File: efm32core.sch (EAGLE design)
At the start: 44 parts, among them U1 IP4220CZ6SSOT-6, X1 48.0MHz, X2 32.768kHz

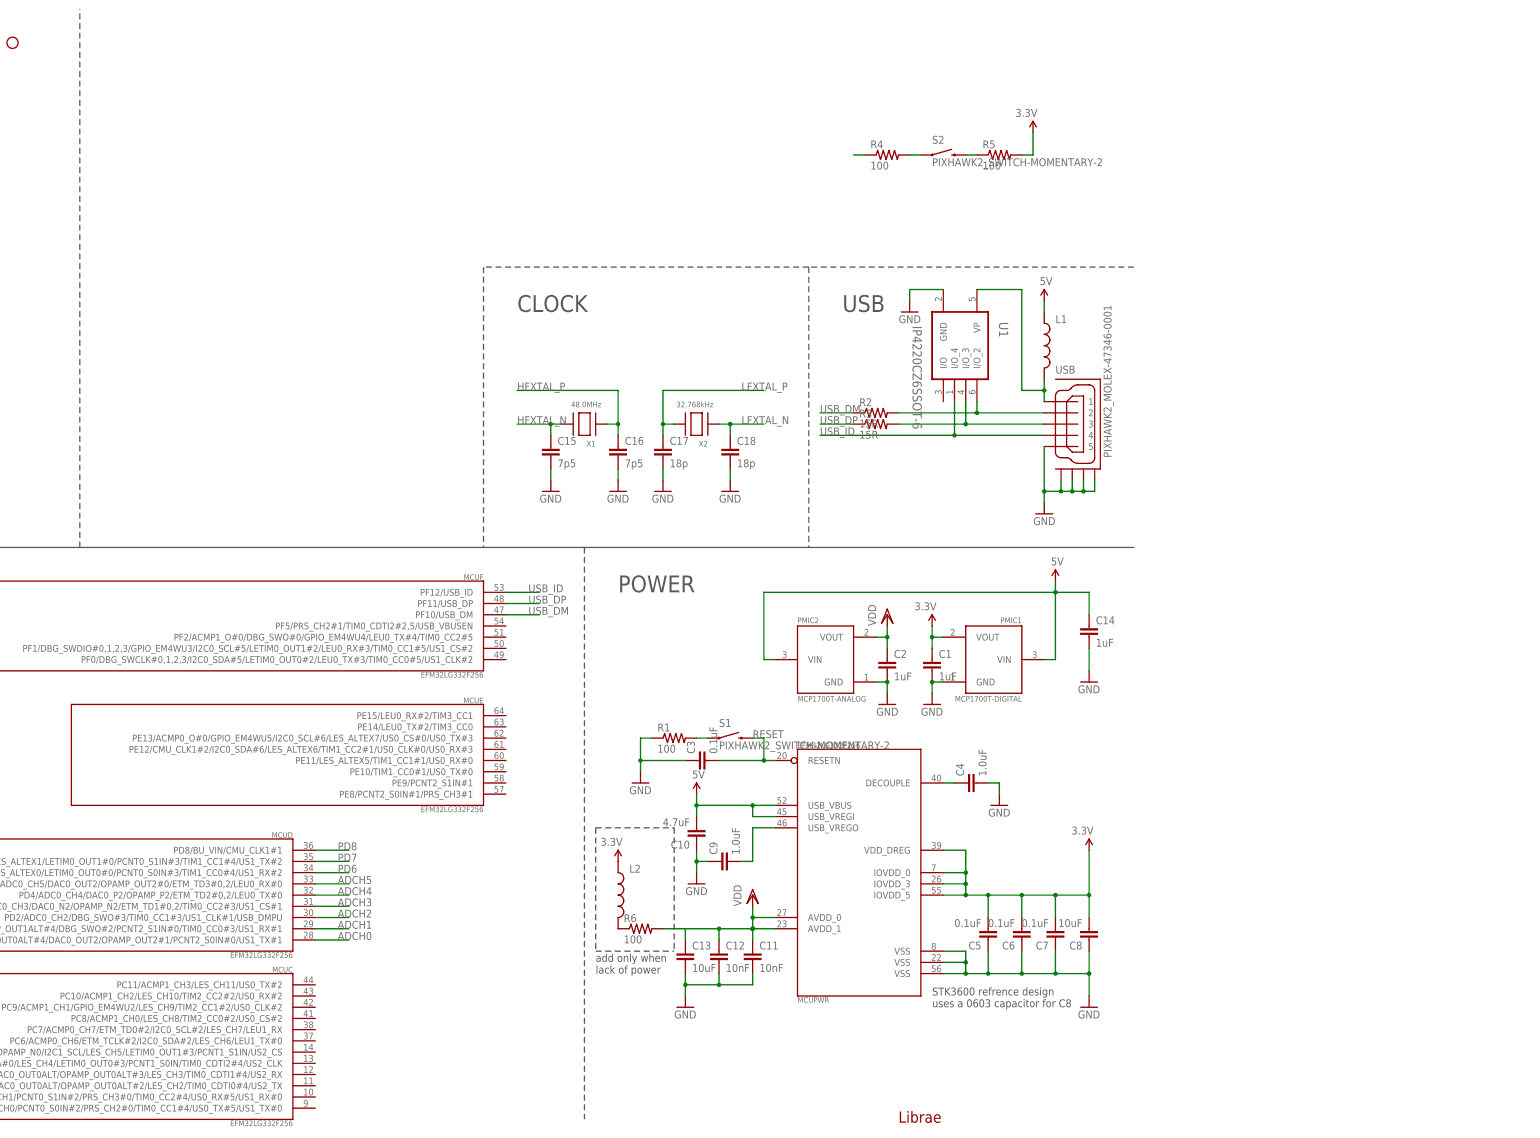
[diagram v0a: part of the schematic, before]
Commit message: add up bluetooth module and microsd socket
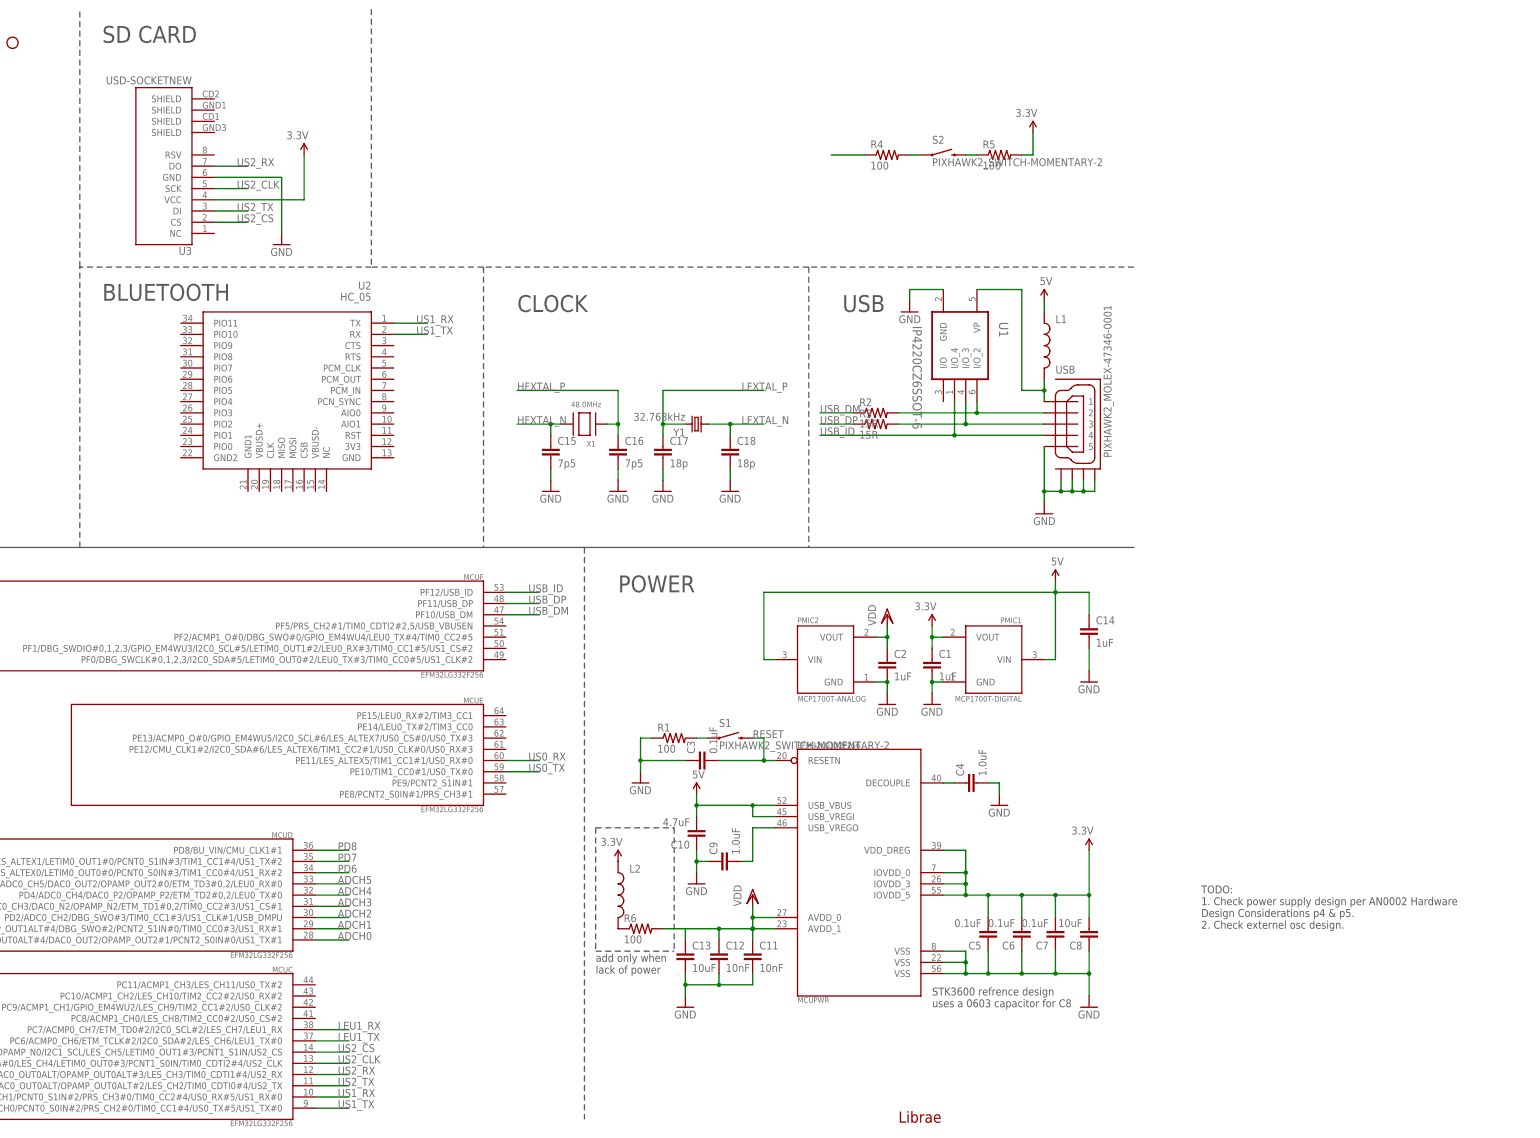
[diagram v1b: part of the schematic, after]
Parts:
- removed X2: 32.768kHz, adafruit:XTALNX5032
- added U2: HC_05, SerialPortBluetooth:HC_05
- added U3: USD-SOCKETNEW, SparkFun-Connectors:USD-SOCKETNEW
- added Y1: 32.768kHz, SparkFun-FreqCtrl:CRYSTAL5X1.5
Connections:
- new net LEU1_RX: MCUC.PC7/ACMP0_CH7/ETM_TD0#2/I2C0_SCL#2/LES_CH7/LEU1_RX
- new net LEU1_TX: MCUC.PC6/ACMP0_CH6/ETM_TCLK#2/I2C0_SDA#2/LES_CH6/LEU1_TX#0
- new net US0_RX: MCUE.PE11/LES_ALTEX5/TIM1_CC1#1/US0_RX#0
- new net US0_TX: MCUE.PE10/TIM1_CC0#1/US0_TX#0
- new net US1_RX: MCUC.PC1/ACMP0_CH1/DAC0_OUT0ALT/OPAMP_OUT0ALT#1/I2C0_SCL#4/LES_CH1/PCNT0_S1IN#2/PRS_CH3#0/TIM0_CC2#4/US0_RX#5/US1_RX#0, U2.TX
- new net US1_TX: MCUC.PC0/ACMP0_CH0/DAC0_OUT0ALT/OPAMP_OUT0ALT#0/I2C0_SDA#4/LES_CH0/PCNT0_S0IN#2/PRS_CH2#0/TIM0_CC1#4/US0_TX#5/US1_TX#0, U2.RX
- new net US2_CLK: MCUC.PC4/ACMP0_CH4/DAC0_P0/OPAMP_P0/I2C1_SDA#0/LES_CH4/LETIM0_OUT0#3/PCNT1_S0IN/TIM0_CDTI2#4/US2_CLK, U3.SCK
- new net US2_CS: MCUC.PC5/ACMP0_CH5/DAC0_N0/OPAMP_N0/I2C1_SCL/LES_CH5/LETIM0_OUT1#3/PCNT1_S1IN/US2_CS, U3.CS
- new net US2_RX: MCUC.PC3/ACMP0_CH3/DAC0_OUT0ALT/OPAMP_OUT0ALT#3/LES_CH3/TIM0_CDTI1#4/US2_RX, U3.DO
- new net US2_TX: MCUC.PC2/ACMP0_CH2/DAC0_OUT0ALT/OPAMP_OUT0ALT#2/LES_CH2/TIM0_CDTI0#4/US2_TX, U3.DI
- net 3.3V: now also U3.VCC
- net GND: now also U3.GND
- net LFXTAL_N: now also Y1.1; no longer X2.P$1
- net LFXTAL_P: now also Y1.2; no longer X2.P$2
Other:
- note added: "BLUETOOTH"
- note added: "SD CARD"
- note added: "TODO: 1. Check power supply design per AN0002 Hardware Design Considerations p4 & p5. 2. Check externel osc design."

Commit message: update a bit
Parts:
- added U4: MPU-6000QFN-24, SparkFun-Sensors:MPU-6000QFN-24
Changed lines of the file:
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@@
 <grid distance="0.1" unitdist="inch" unit="inch" style="lines" multiple="1" display="yes" altdistance="0.01" altunitdist="inch" altunit="inch"/>
 <layers>
-<layer number="1" name="Top" color="4" fill="1" visible="no" active="no"/>
-<layer number="16" name="Bottom" color="1" fill="1" visible="no" active="no"/>
-<layer number="17" name="Pads" color="2" fill="1" visible="no" active="no"/>
-<layer number="18" name="Vias" color="2" fill="1" visible="no" active="no"/>
-<layer number="19" name="Unrouted" color="6" fill="1" visible="no" active="no"/>
-<layer number="20" name="Dimension" color="15" fill="1" visible="no" active="no"/>
-<layer number="21" name="tPlace" color="7" fill="1" visible="no" active="no"/>
-<layer number="22" name="bPlace" color="7" fill="1" visible="no" active="no"/>
-<layer number="23" name="tOrigins" color="15" fill="1" visible="no" active="no"/>
-<layer number="24" name="bOrigins" color="15" fill="1" visible="no" active="no"/>
-<layer number="25" name="tNames" color="7" fill="1" visible="no" active="no"/>
-<layer number="26" name="bNames" color="7" fill="1" visible="no" active="no"/>
-<layer number="27" name="tValues" color="7" fill="1" visible="no" active="no"/>
-<layer number="28" name="bValues" color="7" fill="1" visible="no" active="no"/>
+<layer number="1" name="Top" color="4" fill="1" visible="yes" active="no"/>
+<layer number="16" name="Bottom" color="1" fill="1" visible="yes" active="no"/>
+<layer number="17" name="Pads" color="2" fill="1" visible="yes" active="no"/>
+<layer number="18" name="Vias" color="2" fill="1" visible="yes" active="no"/>
+<layer number="19" name="Unrouted" color="6" fill="1" visible="yes" active="no"/>
+<layer number="20" name="Dimension" color="15" fill="1" visible="yes" active="no"/>
+<layer number="21" name="tPlace" color="7" fill="1" visible="yes" active="no"/>
+<layer number="22" name="bPlace" color="7" fill="1" visible="yes" active="no"/>
+<layer number="23" name="tOrigins" color="15" fill="1" visible="yes" active="no"/>
+<layer number="24" name="bOrigins" color="15" fill="1" visible="yes" active="no"/>
+<layer number="25" name="tNames" color="7" fill="1" visible="yes" active="no"/>
+<layer number="26" name="bNames" color="7" fill="1" visible="yes" active="no"/>
+<layer number="27" name="tValues" color="7" fill="1" visible="yes" active="no"/>
+<layer number="28" name="bValues" color="7" fill="1" visible="yes" active="no"/>
 <layer number="29" name="tStop" color="7" fill="3" visible="no" active="no"/>
 <layer number="30" name="bStop" color="7" fill="6" visible="no" active="no"/>
@@
 <layer number="35" name="tGlue" color="7" fill="4" visible="no" active="no"/>
 <layer number="36" name="bGlue" color="7" fill="5" visible="no" active="no"/>
-<layer number="37" name="tTest" color="7" fill="1" visible="no" active="no"/>
-<layer number="38" name="bTest" color="7" fill="1" visible="no" active="no"/>
+<layer number="37" name="tTest" color="7" fill="1" visible="yes" active="no"/>
+<layer number="38" name="bTest" color="7" fill="1" visible="yes" active="no"/>
 <layer number="39" name="tKeepout" color="4" fill="11" visible="no" active="no"/>
 <layer number="40" name="bKeepout" color="1" fill="11" visible="no" active="no"/>
@@
 <layer number="44" name="Drills" color="7" fill="1" visible="no" active="no"/>
 <layer number="45" name="Holes" color="7" fill="1" visible="no" active="no"/>
-<layer number="46" name="Milling" color="3" fill="1" visible="no" active="no"/>
-<layer number="47" name="Measures" color="7" fill="1" visible="no" active="no"/>
-<layer number="48" name="Document" color="7" fill="1" visible="no" active="no"/>
-<layer number="49" name="Reference" color="7" fill="1" visible="no" active="no"/>
-<layer number="50" name="dxf" color="7" fill="1" visible="no" active="no"/>
-<layer number="51" name="tDocu" color="14" fill="1" visible="no" active="no"/>
-<layer number="52" name="bDocu" color="6" fill="1" visible="no" active="no"/>
-<layer number="53" name="tGND_GNDA" color="7" fill="9" visible="no" active="no"/>
-<layer number="54" name="bGND_GNDA" color="1" fill="9" visible="no" active="no"/>
-<layer number="56" name="wert" color="7" fill="1" visible="no" active="no"/>
-<layer number="57" name="tCAD" color="7" fill="1" visible="no" active="no"/>
-<layer number="58" name="bCAD" color="7" fill="1" visible="no" active="no"/>
+<layer number="46" name="Milling" color="3" fill="1" visible="yes" active="no"/>
+<layer number="47" name="Measures" color="7" fill="1" visible="yes" active="no"/>
+<layer number="48" name="Document" color="7" fill="1" visible="yes" active="no"/>
+<layer number="49" name="Reference" color="7" fill="1" visible="yes" active="no"/>
+<layer number="50" name="dxf" color="7" fill="1" visible="yes" active="no"/>
+<layer number="51" name="tDocu" color="14" fill="1" visible="yes" active="no"/>
+<layer number="52" name="bDocu" color="6" fill="1" visible="yes" active="no"/>
+<layer number="53" name="tGND_GNDA" color="7" fill="9" visible="yes" active="no"/>
+<layer number="54" name="bGND_GNDA" color="1" fill="9" visible="yes" active="no"/>
+<layer number="56" name="wert" color="7" fill="1" visible="yes" active="no"/>
+<layer number="57" name="tCAD" color="7" fill="1" visible="yes" active="no"/>
+<layer number="58" name="bCAD" color="7" fill="1" visible="yes" active="no"/>
 <layer number="91" name="Nets" color="2" fill="1" visible="yes" active="yes"/>
 <layer number="92" name="Busses" color="1" fill="1" visible="yes" active="yes"/>
@@
 <part name="GND15" library="SparkFun-Aesthetics" deviceset="GND" device=""/>
 <part name="3.3V4" library="SparkFun-Aesthetics" deviceset="3.3V" device=""/>
+<part name="U4" library="SparkFun-Sensors" deviceset="MPU-6000" device="QFN-24"/>
 </parts>
 <sheets>
@@
 <instance part="GND15" gate="1" x="190.5" y="203.2"/>
 <instance part="3.3V4" gate="G$1" x="195.58" y="223.52" rot="MR0"/>
+<instance part="U4" gate="G$1" x="243.84" y="231.14"/>
 </instances>
 <busses>

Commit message: complete connections
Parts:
- removed U4: MPU-6000QFN-24, SparkFun-Sensors:MPU-6000QFN-24
- added C19: 10nF, SparkFun-Capacitors:10NF/10000PF-50V-10%(0603)
- added C20, C21: 0.1uF, SparkFun-Capacitors:0.1UF-25V(+80/-20%)(0603)
- added C22: 2.2uF, SparkFun-Capacitors:2.2UF-10V-20%(0603)
- added MPU9150: (no value), SparkFun-Sensors:MPU-9150QFN-24-NP
- added R7, R8: 4.7k, SparkFun-Resistors:100OHM1/10W1%(0603)
- R4: value 100 -> 10k
- R5: value 100 -> 1k
- S2: value PIXHAWK2_SWITCH-MOMENTARY-2 -> BUTTON
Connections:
- removed net N$2: R4.2, S2.1
- removed net N$5: R4.1
- removed net PA0: MCUA.PA0/GPIO_EM4WU0/I2C0_SDA#0/LEU0_RX#4/PRS_CH0/TIM0_CC0#0,1,4
- new net I2C0_SCL: MCUA.PA1/CMU_CLK1#0/I2C0_SCL#0/PRS_CH1/TIM0_CC1#0,1, MPU9150.SCL, R8.1
- new net I2C0_SDA: MCUA.PA0/GPIO_EM4WU0/I2C0_SDA#0/LEU0_RX#4/PRS_CH0/TIM0_CC0#0,1,4, MPU9150.SDA, R7.1
- new net N$12: C21.2, MPU9150.REGOUT
- new net N$15: C22.1, MPU9150.CPOUT
- new net PA2: MCUA.PA2/CMU_CLK0#0/ETM_TD0#3/TIM0_CC2#0,1, R4.2, S2.1
- net 3.3V: now also C19.2, C20.2, MPU9150.VDD@13, MPU9150.VDD@3, MPU9150.VLOGIC, R7.2, R8.2
- net GND: now also C19.1, C20.1, C21.1, C22.2, MPU9150.GND@15, MPU9150.GND@17, MPU9150.GND@18, R4.1
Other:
- note added: "BUTTON"
- moved on the sheet: R4, R5, S2, U2, U3
